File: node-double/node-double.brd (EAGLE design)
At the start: 33.3 x 24.1 mm, 29 parts, among them IC1 TP4056, IC3 24C02, U1 ATMEGA328P_TQFP, U2 3.3V/150mA

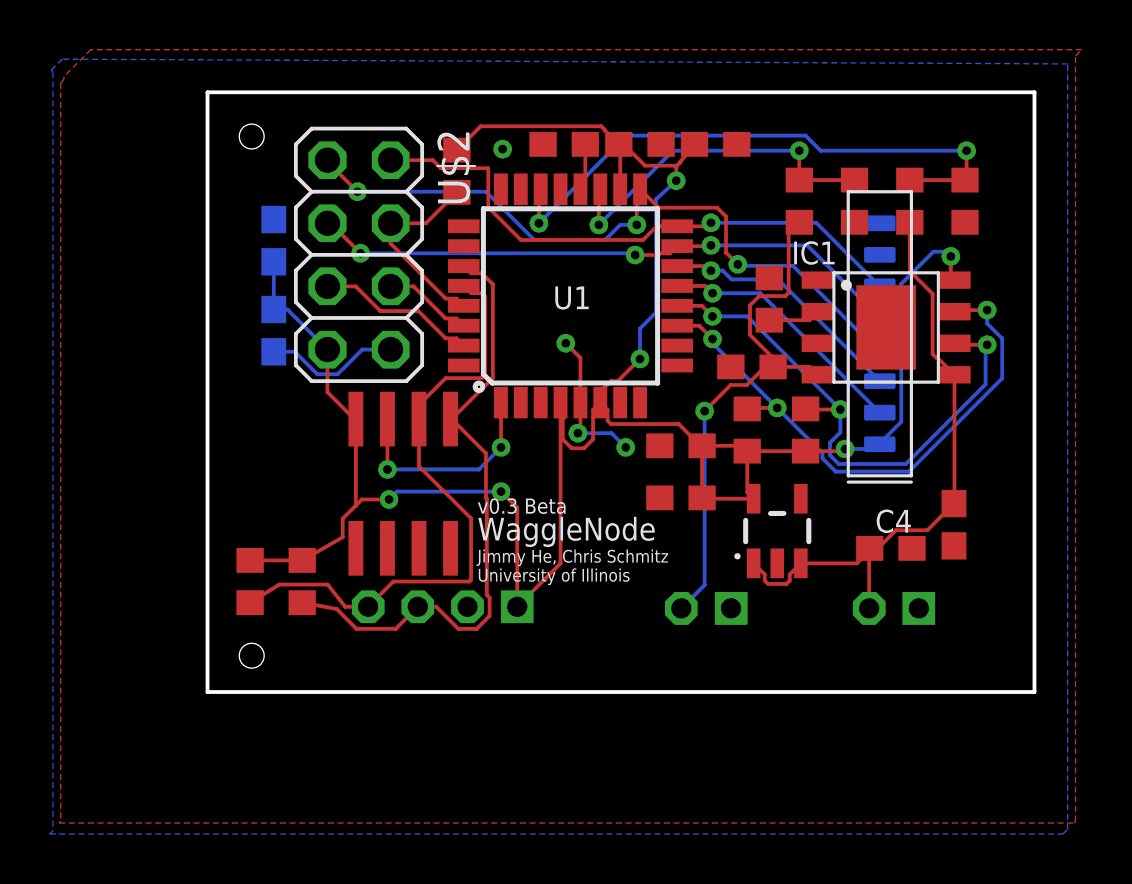
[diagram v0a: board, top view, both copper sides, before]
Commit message: Revert "Router PCB"
This reverts commit 5cfdc418179729a7dd419c7a517ca3d373416e11.
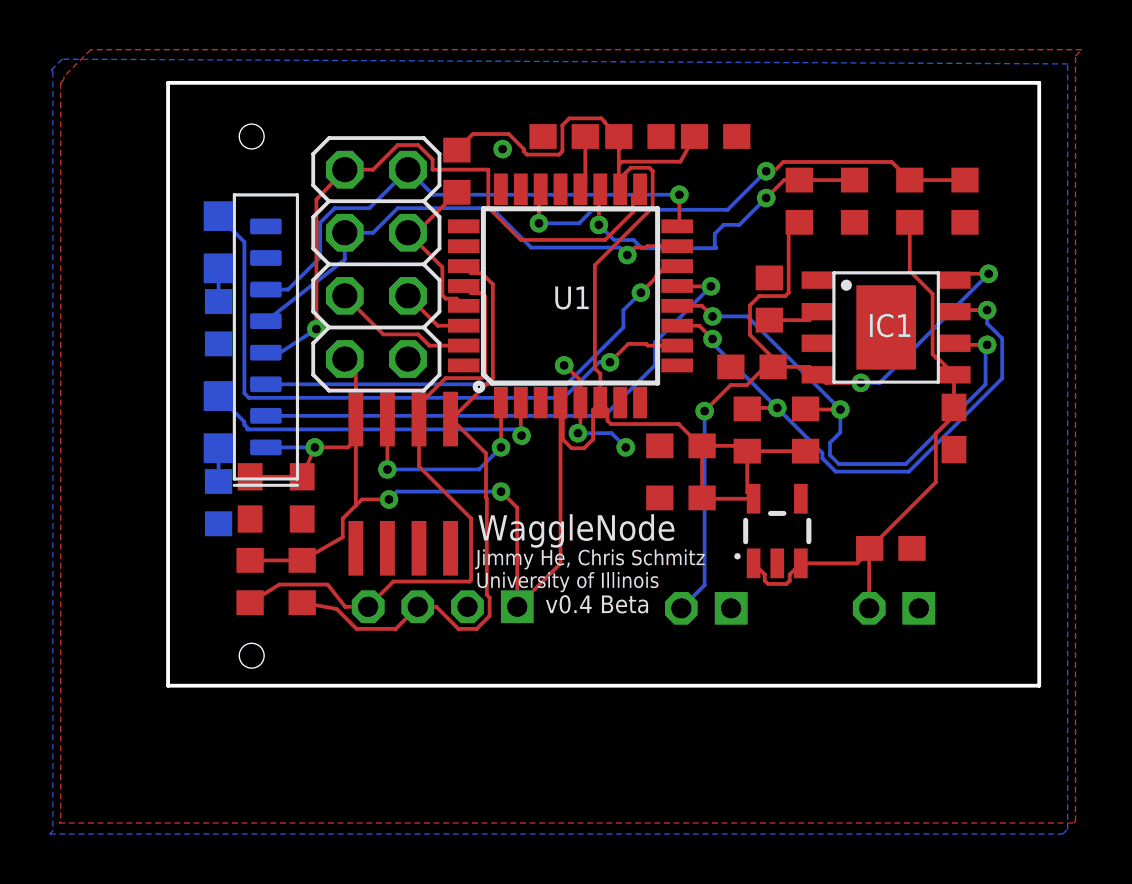
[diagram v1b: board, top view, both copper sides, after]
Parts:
- added LED1, LED2: (no value), led:SML0805
- added R2, R3: 1K, resistor:R0603
- moved U$1 24.7 mm to (23.3, 30.1)
- moved C10 10.4 mm to (23.9, 28.1), flipped to the top, turned to 270 degrees
- moved C8 6.83 mm to (26.0, 28.1), flipped to the top
- moved C3 3.87 mm to (52.3, 30.9)
- moved U$2 0.80 mm to (29.0, 37.5)
- moved C1 0.32 mm to (36.6, 42.6)
- moved C7 0.32 mm to (39.6, 42.6)
- moved C9 0.32 mm to (42.7, 42.6)
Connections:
- new net N$1: LED1.C, R2.1
- new net N$2: LED2.C, R3.1
- net D4: now also LED1.A
- net D6: now also LED2.A
- net GND: now also R2.2, R3.2
- net VCC: no longer IC1.8
- net VIN: now also IC1.8
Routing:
- net D6: track 0.00 -> 26.0 mm, vias 0 -> 1
- net D4: track 0.00 -> 14.4 mm, vias 0 -> 1
- net D9: track 10.3 -> 22.0 mm
- net VIN: track 21.4 -> 31.7 mm, vias 1 -> 3
- net D10: track 10.1 -> 19.0 mm
- net VCC: track 95.2 -> 87.3 mm, vias 6 -> 3
- net GND: track 11.6 -> 5.22 mm
- net MOSI/11: track 24.1 -> 19.8 mm, vias 3 -> 1
- net A7: track 23.8 -> 20.0 mm
- net SCK/13: track 28.7 -> 25.4 mm, vias 3 -> 1
- net MISO/12: track 23.3 -> 21.2 mm
- net N$2: track 0.00 -> 1.34 mm
- net N$1: track 0.00 -> 1.34 mm
- net RST: track 7.98 -> 6.77 mm
- net TX-0: track 6.47 -> 5.62 mm
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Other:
- board size 33.3 x 24.1 mm -> 35.1 x 24.3 mm
- board text added: "v0.4 Beta"
- board text removed: "v0.3 Beta"

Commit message: Router PCB
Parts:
- removed LED1, LED2: (no value), led:SML0805
- removed R2, R3: 1K, resistor:R0603
- moved U$1 24.7 mm to (48.0, 30.2)
- moved C10 10.4 mm to (24.9, 38.4), flipped to the bottom, turned to 90 degrees
- moved C8 6.83 mm to (24.9, 34.8), flipped to the bottom
- moved C3 3.87 mm to (52.3, 27.0)
- moved U$2 0.80 mm to (28.3, 37.8)
- moved C1 0.32 mm to (36.6, 42.3)
- moved C7 0.32 mm to (39.6, 42.3)
- moved C9 0.32 mm to (42.7, 42.3)
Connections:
- removed net N$1: LED1.C, R2.1
- removed net N$2: LED2.C, R3.1
- net D4: no longer LED1.A
- net D6: no longer LED2.A
- net GND: no longer R2.2, R3.2
- net VCC: now also IC1.8
- net VIN: no longer IC1.8
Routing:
- net D6: track 26.0 -> 0.00 mm, vias 1 -> 0
- net D4: track 14.4 -> 0.00 mm, vias 1 -> 0
- net D9: track 22.0 -> 10.3 mm
- net VIN: track 31.7 -> 21.4 mm, vias 3 -> 1
- net D10: track 19.0 -> 10.1 mm
- net VCC: track 87.3 -> 95.2 mm, vias 3 -> 6
- net GND: track 5.22 -> 11.6 mm
- net MOSI/11: track 19.8 -> 24.1 mm, vias 1 -> 3
- net A7: track 20.0 -> 23.8 mm
- net SCK/13: track 25.4 -> 28.7 mm, vias 1 -> 3
- net MISO/12: track 21.2 -> 23.3 mm
- net N$2: track 1.34 -> 0.00 mm
- net N$1: track 1.34 -> 0.00 mm
- net RST: track 6.77 -> 7.98 mm
- net TX-0: track 5.62 -> 6.47 mm
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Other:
- board size 35.1 x 24.3 mm -> 33.3 x 24.1 mm
- board text added: "v0.3 Beta"
- board text removed: "v0.4 Beta"

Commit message: Node: v4
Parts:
- added LED1, LED2: (no value), led:SML0805
- added R2, R3: 1K, resistor:R0603
- moved U$1 24.7 mm to (23.3, 30.1)
- moved C10 10.4 mm to (23.9, 28.1), flipped to the top, turned to 270 degrees
- moved C8 6.83 mm to (26.0, 28.1), flipped to the top
- moved C3 3.87 mm to (52.3, 30.9)
- moved U$2 0.80 mm to (29.0, 37.5)
- moved C1 0.32 mm to (36.6, 42.6)
- moved C7 0.32 mm to (39.6, 42.6)
- moved C9 0.32 mm to (42.7, 42.6)
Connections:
- new net N$1: LED1.C, R2.1
- new net N$2: LED2.C, R3.1
- net D4: now also LED1.A
- net D6: now also LED2.A
- net GND: now also R2.2, R3.2
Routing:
- net D6: track 0.00 -> 26.0 mm, vias 0 -> 1
- net D4: track 0.00 -> 14.4 mm, vias 0 -> 1
- net D9: track 10.3 -> 22.0 mm
- net D10: track 10.1 -> 19.0 mm
- net GND: track 11.6 -> 5.22 mm
- net VCC: track 95.2 -> 100.4 mm, vias 6 -> 5
- net MOSI/11: track 24.1 -> 19.8 mm, vias 3 -> 1
- net A7: track 23.8 -> 20.0 mm
- net SCK/13: track 28.7 -> 25.4 mm, vias 3 -> 1
- net MISO/12: track 23.3 -> 21.2 mm
- net N$2: track 0.00 -> 1.34 mm
- net N$1: track 0.00 -> 1.34 mm
- net RST: track 7.98 -> 6.77 mm
- net TX-0: track 6.47 -> 5.62 mm
- net RX-1: track 3.60 -> 2.74 mm
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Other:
- board size 33.3 x 24.1 mm -> 35.1 x 24.3 mm
- board text added: "v0.4 Beta"
- board text removed: "v0.3 Beta"

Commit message: Node: Tweaked TP4056 activation point
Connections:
- net VCC: no longer IC1.8
- net VIN: now also IC1.8
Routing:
- net VCC: track 100.4 -> 87.3 mm, vias 5 -> 3
- net VIN: track 21.4 -> 31.7 mm, vias 1 -> 3
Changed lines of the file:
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@@
 <grid distance="2.5" unitdist="mil" unit="mil" style="lines" multiple="1" display="yes" altdistance="10" altunitdist="mil" altunit="mil"/>
 <layers>
-<layer number="1" name="Top" color="4" fill="1" visible="no" active="yes"/>
+<layer number="1" name="Top" color="4" fill="1" visible="yes" active="yes"/>
 <layer number="2" name="Route2" color="1" fill="3" visible="no" active="no"/>
 <layer number="3" name="Route3" color="4" fill="3" visible="no" active="no"/>
@@
 <layer number="19" name="Unrouted" color="6" fill="1" visible="yes" active="yes"/>
 <layer number="20" name="Dimension" color="24" fill="1" visible="yes" active="yes"/>
-<layer number="21" name="tPlace" color="7" fill="1" visible="no" active="yes"/>
+<layer number="21" name="tPlace" color="7" fill="1" visible="yes" active="yes"/>
 <layer number="22" name="bPlace" color="7" fill="1" visible="yes" active="yes"/>
-<layer number="23" name="tOrigins" color="15" fill="1" visible="no" active="yes"/>
+<layer number="23" name="tOrigins" color="15" fill="1" visible="yes" active="yes"/>
 <layer number="24" name="bOrigins" color="15" fill="1" visible="yes" active="yes"/>
-<layer number="25" name="tNames" color="7" fill="1" visible="no" active="yes"/>
+<layer number="25" name="tNames" color="7" fill="1" visible="yes" active="yes"/>
 <layer number="26" name="bNames" color="7" fill="1" visible="yes" active="yes"/>
-<layer number="27" name="tValues" color="7" fill="1" visible="no" active="yes"/>
-<layer number="28" name="bValues" color="7" fill="1" visible="no" active="yes"/>
+<layer number="27" name="tValues" color="7" fill="1" visible="yes" active="yes"/>
+<layer number="28" name="bValues" color="7" fill="1" visible="yes" active="yes"/>
 <layer number="29" name="tStop" color="7" fill="3" visible="no" active="yes"/>
 <layer number="30" name="bStop" color="7" fill="6" visible="no" active="yes"/>
@@
 <layer number="37" name="tTest" color="7" fill="1" visible="no" active="yes"/>
 <layer number="38" name="bTest" color="7" fill="1" visible="no" active="yes"/>
-<layer number="39" name="tKeepout" color="4" fill="11" visible="no" active="yes"/>
+<layer number="39" name="tKeepout" color="4" fill="11" visible="yes" active="yes"/>
 <layer number="40" name="bKeepout" color="1" fill="11" visible="yes" active="yes"/>
-<layer number="41" name="tRestrict" color="4" fill="10" visible="no" active="yes"/>
+<layer number="41" name="tRestrict" color="4" fill="10" visible="yes" active="yes"/>
 <layer number="42" name="bRestrict" color="1" fill="10" visible="yes" active="yes"/>
 <layer number="43" name="vRestrict" color="2" fill="10" visible="no" active="yes"/>
-<layer number="44" name="Drills" color="7" fill="1" visible="no" active="yes"/>
+<layer number="44" name="Drills" color="7" fill="1" visible="yes" active="yes"/>
 <layer number="45" name="Holes" color="7" fill="1" visible="yes" active="yes"/>
 <layer number="46" name="Milling" color="3" fill="1" visible="no" active="yes"/>
@@
 <layer number="49" name="Reference" color="7" fill="1" visible="no" active="yes"/>
 <layer number="50" name="dxf" color="7" fill="1" visible="no" active="no"/>
-<layer number="51" name="tDocu" color="7" fill="1" visible="no" active="yes"/>
+<layer number="51" name="tDocu" color="7" fill="1" visible="yes" active="yes"/>
 <layer number="52" name="bDocu" color="7" fill="1" visible="yes" active="yes"/>
 <layer number="53" name="tGND_GNDA" color="7" fill="9" visible="no" active="no"/>
@@
 <contactref element="U1" pad="6"/>
 <contactref element="R5" pad="2"/>
-<contactref element="IC1" pad="8"/>
 <contactref element="R4" pad="2"/>
 <contactref element="C7" pad="1"/>
@@
 <wire x1="39.0332" y1="41.1284875" x2="39.0332" y2="40.6908" width="0.1524" layer="1"/>
 <wire x1="39.0332" y1="40.6908" x2="38.83" y2="40.4876" width="0.1524" layer="1"/>
-<wire x1="52.28" y1="36.83" x2="53.721" y2="36.83" width="0.1524" layer="1"/>
-<wire x1="53.721" y1="36.83" x2="53.7845" y2="36.8935" width="0.1524" layer="1"/>
-<via x="53.7845" y="36.8935" extent="1-16" drill="0.35"/>
-<wire x1="53.7845" y1="36.8935" x2="48.895" y2="32.004" width="0.1524" layer="16"/>
-<wire x1="48.895" y1="32.004" x2="48.895" y2="30.0355" width="0.1524" layer="16"/>
-<via x="48.895" y="30.0355" extent="1-16" drill="0.35"/>
-<wire x1="48.895" y1="30.0355" x2="48.807" y2="29.9475" width="0.1524" layer="1"/>
-<wire x1="48.807" y1="29.9475" x2="46.2915" y2="29.9475" width="0.1524" layer="1"/>
 </signal>
 <signal name="RST">
@@
 <wire x1="42.2275" y1="31.5595" x2="42.2275" y2="24.5585" width="0.1524" layer="16"/>
 <wire x1="42.2275" y1="24.5585" x2="41.291" y2="23.622" width="0.1524" layer="16"/>
+<contactref element="IC1" pad="8"/>
+<wire x1="52.28" y1="36.83" x2="52.534" y2="37.084" width="0.1524" layer="1"/>
+<wire x1="52.534" y1="37.084" x2="53.6575" y2="37.084" width="0.1524" layer="1"/>
+<via x="53.6575" y="37.084" extent="1-16" drill="0.35"/>
+<wire x1="53.6575" y1="37.084" x2="49.2679" y2="32.6944" width="0.1524" layer="16"/>
+<wire x1="49.2679" y1="32.6944" x2="48.514" y2="32.6944" width="0.1524" layer="16"/>
+<via x="48.514" y="32.6944" extent="1-16" drill="0.35"/>
+<wire x1="48.514" y1="32.6944" x2="47.1056" y2="32.6944" width="0.1524" layer="1"/>
+<wire x1="47.1056" y1="32.6944" x2="46.78" y2="33.02" width="0.1524" layer="1"/>
 </signal>
 <signal name="PROG">
